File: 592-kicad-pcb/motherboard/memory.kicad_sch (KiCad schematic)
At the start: 11 parts, among them U11 SD Card Holder, U16 W25Q32JVZP

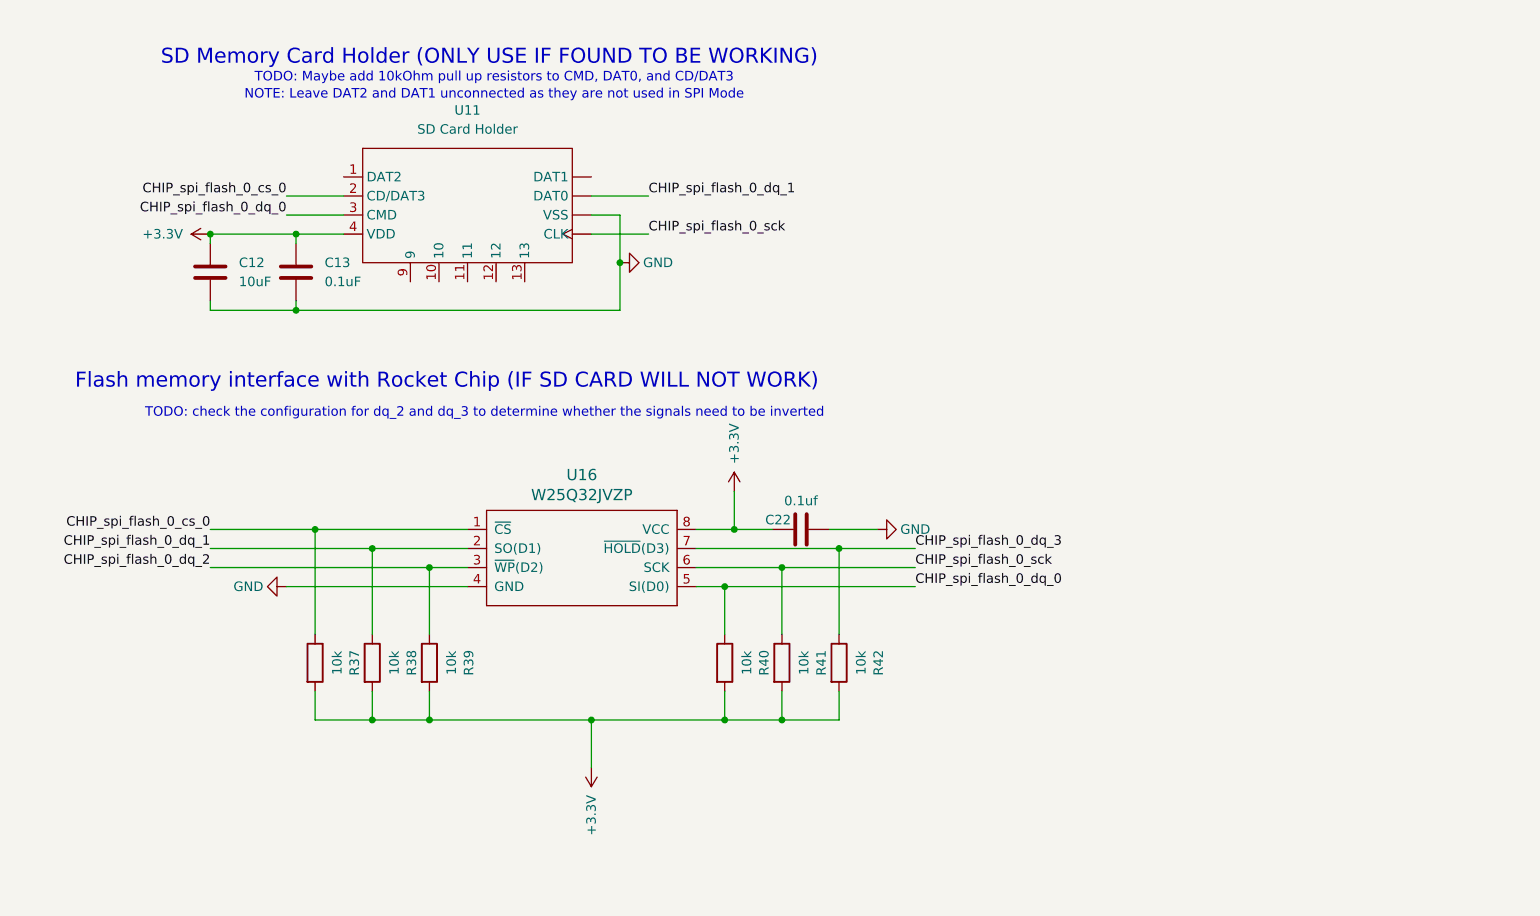
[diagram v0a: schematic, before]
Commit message: combine hierarchy of all sans power
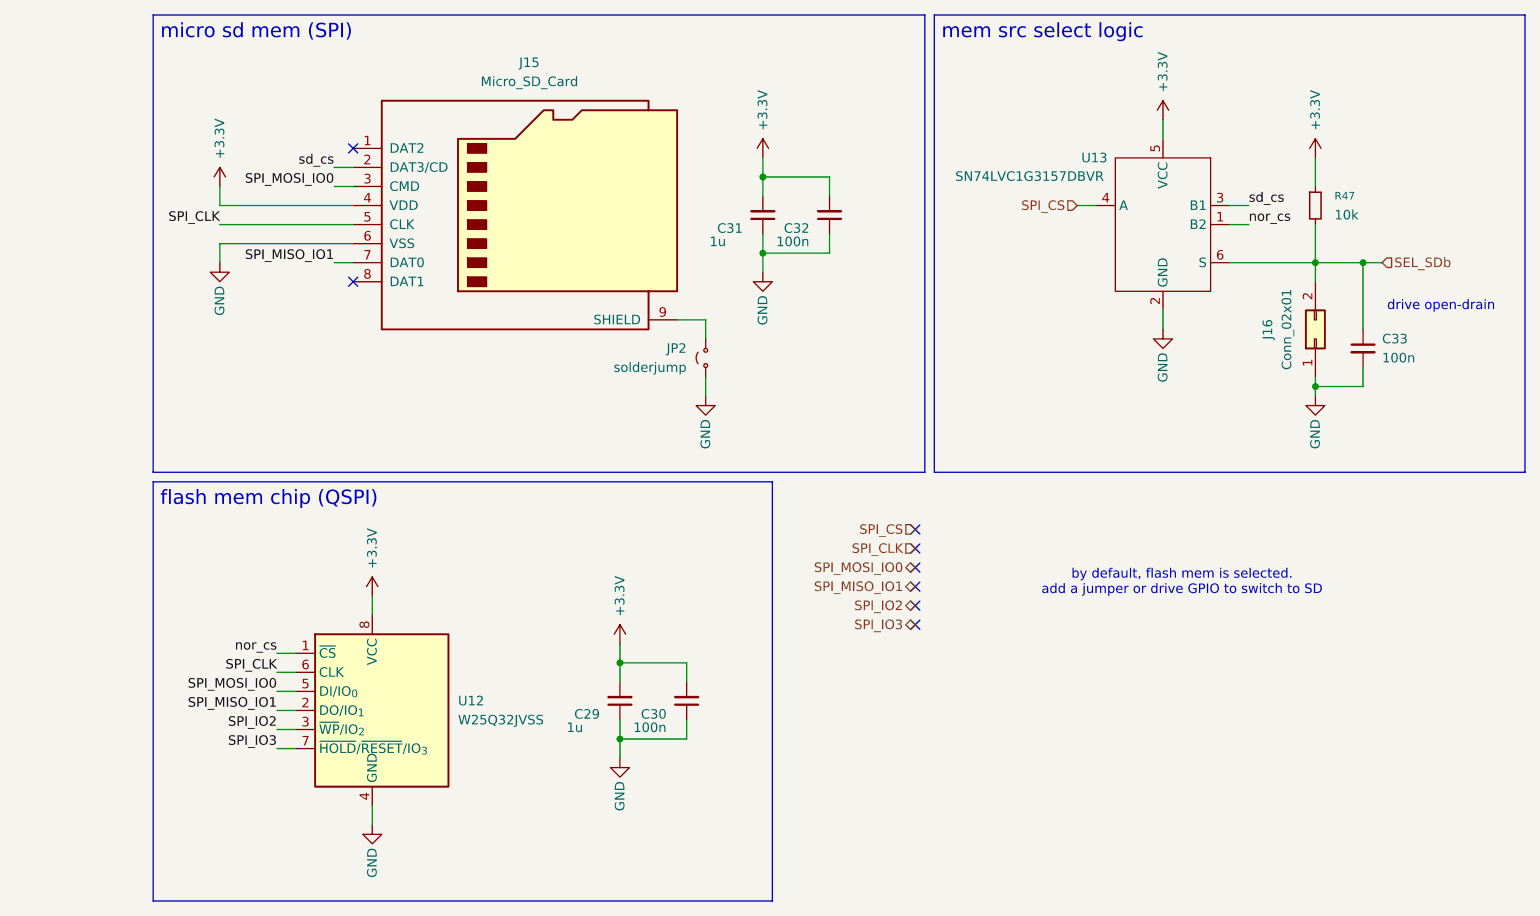
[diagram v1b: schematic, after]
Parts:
- removed C12: 10uF, symbol Device:C
- removed C13: 0.1uF, symbol Device:C
- removed C22: 0.1uf, Capacitor_SMD:C_0805_2012Metric, symbol Device:C
- removed R37, R38, R39, R40, R41, R42: 10k, Resistor_SMD:R_0805_2012Metric, symbol Device:R
- removed U11: SD Card Holder, symbol New_Library:sd_card_connector
- removed U16: W25Q32JVZP, strive_foot_prints:SOIC127P790X216-8N, symbol Caravel_board:W25Q32FVSS
- added C29, C31: 1u, symbol Device:C_Small
- added C30, C32, C33: 100n, symbol Device:C_Small
- added J15: Micro_SD_Card, symbol Connector:Micro_SD_Card
- added J16: Conn_02x01, symbol Connector_Generic:Conn_02x01
- added JP2: solderjump, symbol Jumper:Jumper_2_Small_Open
- added R47: 10k, symbol Device:R_Small
- added U12: W25Q32JVSS, Package_SO:SOIC-8_5.3x5.3mm_P1.27mm, symbol Memory_Flash:W25Q32JVSS
- added U13: SN74LVC1G3157DBVR, Package_TO_SOT_SMD:SOT-23-6, symbol 592-partslib:SN74LVC1G3157DBVR
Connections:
- net +3.3V: now also C29.2, C30.2, C31.2, C32.2, J15.4 (VDD), R47.1, U12.8 (VCC), U13.5 (VCC)
- net GND: now also C29.1, C30.1, C31.1, C32.1, C33.2, J15.6 (VSS), J16.1 (Pin_1), JP2.1 (A), U12.4 (GND), U13.2 (GND)
- new net: J15.9 (SHIELD), JP2.2 (B)
- new net SEL_SDb: C33.1, J16.2 (Pin_2), R47.2, U13.6 (S)
- new net SPI_CLK: J15.5 (CLK), U12.6 (CLK)
- new net SPI_CS: U13.4 (A)
- new net SPI_IO2: U12.3 (~{WP}/IO_{2})
- new net SPI_IO3: U12.7 (~{HOLD}/~{RESET}/IO_{3})
- new net SPI_MISO_IO1: J15.7 (DAT0), U12.2 (DO/IO_{1})
- new net SPI_MOSI_IO0: J15.3 (CMD), U12.5 (DI/IO_{0})
- new net nor_cs: U12.1 (~{CS}), U13.1 (B2)
- new net sd_cs: J15.2 (DAT3/CD), U13.3 (B1)
- no-connect marks 0 -> 8
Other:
- note added: "by default, flash mem is selected. add a jumper or drive GPIO to switch to SD"
- note added: "drive open-drain"
- note removed: "Flash memory interface with Rocket Chip (IF SD CARD WILL NOT WORK)"
- note removed: "NOTE: Leave DAT2 and DAT1 unconnected as they are not used in SPI Mode"
- note removed: "SD Memory Card Holder (ONLY USE IF FOUND TO BE WORKING)"
- note removed: "TODO: Maybe add 10kOhm pull up resistors to CMD, DAT0, and CD/DAT3"
- note removed: "TODO: check the configuration for dq_2 and dq_3 to determine whether the signals need to be inverted"

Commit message: partial update to use STM board, updated muxing of FTDI
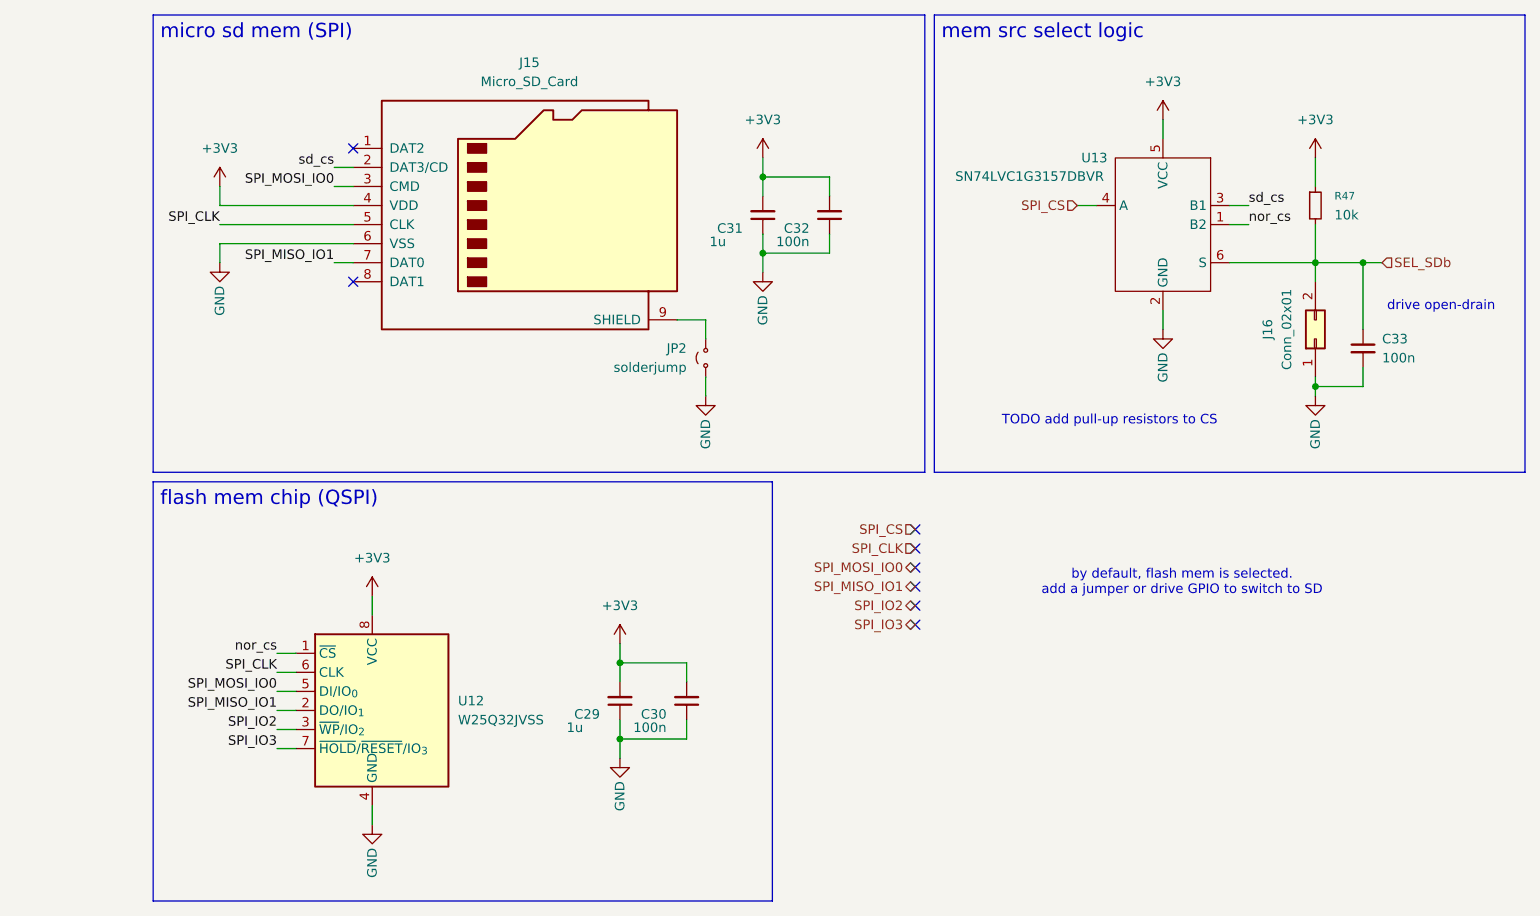
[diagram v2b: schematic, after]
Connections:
- net +3.3V renamed +3V3
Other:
- note added: "TODO add pull-up resistors to CS"

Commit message: update FTDI interfacing
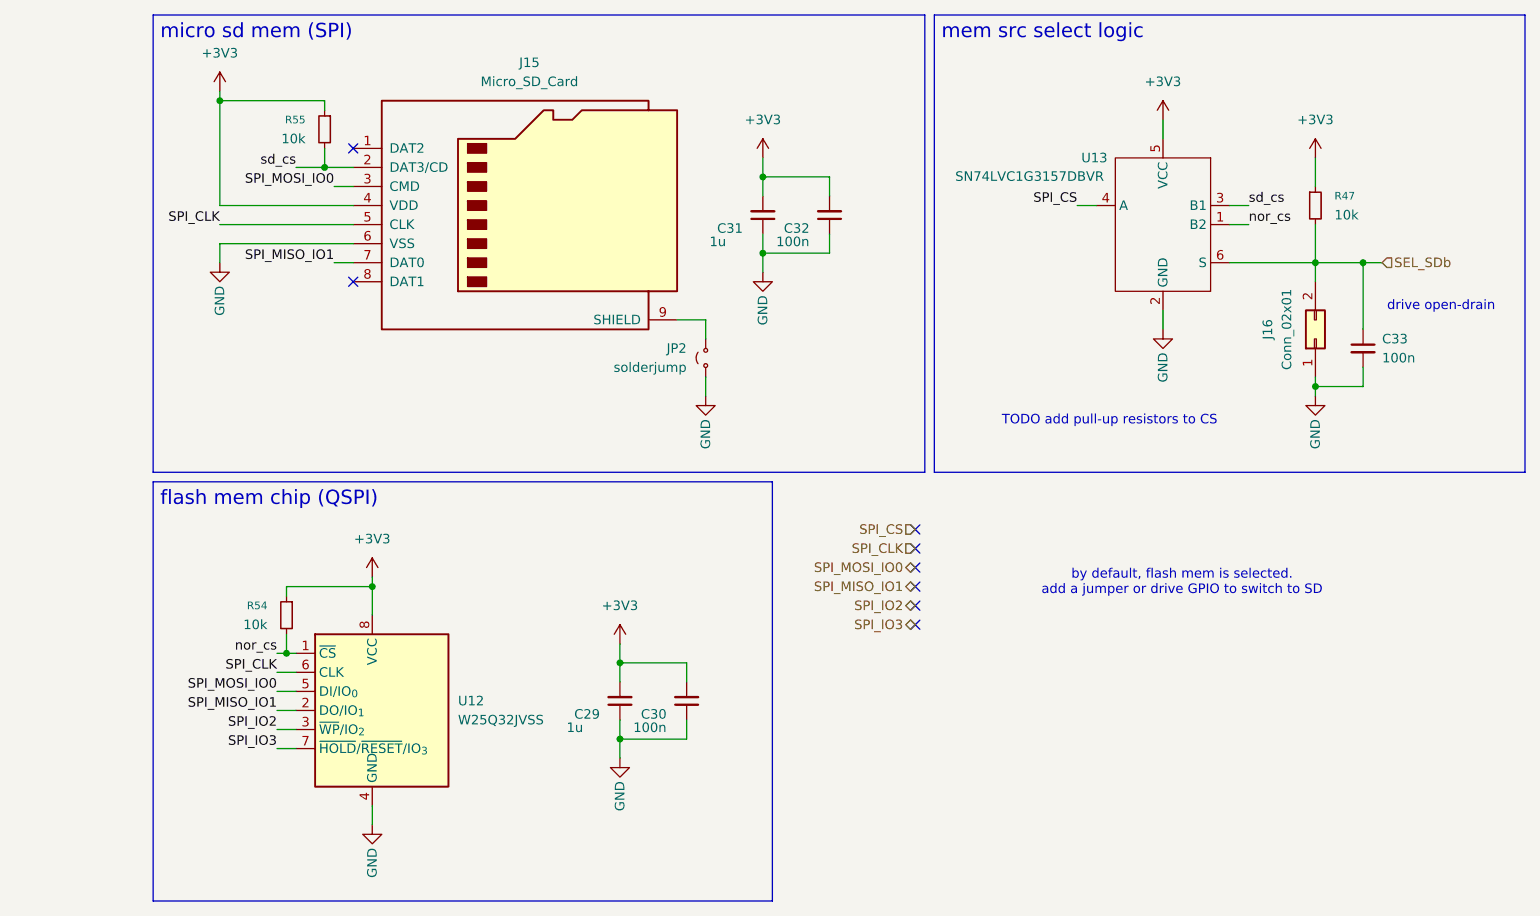
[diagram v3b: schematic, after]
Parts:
- added R54, R55: 10k, symbol Device:R_Small
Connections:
- net +3V3: now also R54.1, R55.1
- net nor_cs: now also R54.2
- net sd_cs: now also R55.2

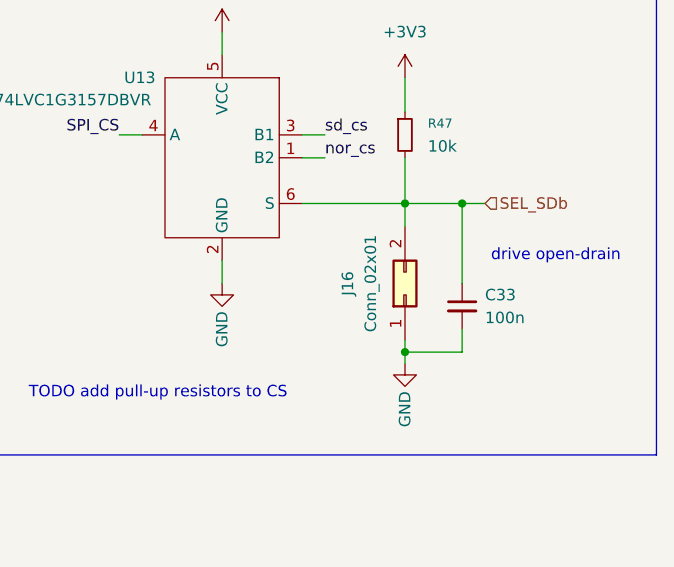
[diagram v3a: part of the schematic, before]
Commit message: add JLC part num for parts, footprints
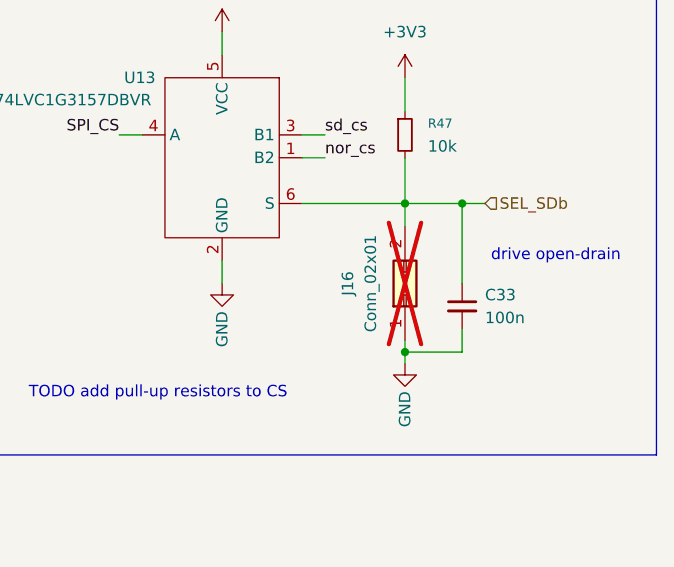
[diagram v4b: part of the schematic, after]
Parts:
- C29, C31: footprint (none) -> Capacitor_SMD:C_0603_1608Metric; LCSC (none) -> C15849
- C30, C32, C33: footprint (none) -> Capacitor_SMD:C_0402_1005Metric; LCSC (none) -> C1525
- J15: footprint (none) -> Connector_Card:microSD_HC_Hirose_DM3AT-SF-PEJM5; LCSC (none) -> C114218
- J16: footprint (none) -> Connector_PinHeader_1.27mm:PinHeader_1x02_P1.27mm_Vertical; now not fitted
- JP2: footprint (none) -> Jumper:SolderJumper-2_P1.3mm_Open_RoundedPad1.0x1.5mm
- R47, R54, R55: footprint (none) -> Resistor_SMD:R_0402_1005Metric; LCSC (none) -> C25744
- U12: LCSC (none) -> C82344
- U13: LCSC (none) -> C10426
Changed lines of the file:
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@@
 			)
 		)
-		(property "Footprint" ""
+		(property "Footprint" "Capacitor_SMD:C_0402_1005Metric"
 			(at 199.39 82.55 0)
 			(effects
@@
 			)
 		)
+		(property "LCSC" "C1525"
+			(at 199.39 82.55 0)
+			(effects
+				(font
+					(size 1.27 1.27)
+				)
+				(hide yes)
+			)
+		)
 		(pin "2"
 		)
@@
 			)
 		)
-		(property "Footprint" ""
+		(property "Footprint" "Capacitor_SMD:C_0603_1608Metric"
 			(at 119.38 64.77 0)
 			(effects
@@
 		)
 		(property "Description" "Unpolarized capacitor, small symbol"
+			(at 119.38 64.77 0)
+			(effects
+				(font
+					(size 1.27 1.27)
+				)
+				(hide yes)
+			)
+		)
+		(property "LCSC" "C15849"
 			(at 119.38 64.77 0)
 			(effects
@@
 			)
 		)
-		(property "Footprint" ""
+		(property "Footprint" "Resistor_SMD:R_0402_1005Metric"
 			(at 193.04 63.5 0)
 			(effects
@@
 			)
 		)
+		(property "LCSC" "C25744"
+			(at 193.04 63.5 0)
+			(effects
+				(font
+					(size 1.27 1.27)
+				)
+				(hide yes)
+			)
+		)
 		(pin "2"
 		)
@@
 			)
 		)
-		(property "Footprint" ""
+		(property "Footprint" "Capacitor_SMD:C_0603_1608Metric"
 			(at 100.33 129.54 0)
 			(effects
@@
 		)
 		(property "Description" "Unpolarized capacitor, small symbol"
+			(at 100.33 129.54 0)
+			(effects
+				(font
+					(size 1.27 1.27)
+				)
+				(hide yes)
+			)
+		)
+		(property "LCSC" "C15849"
 			(at 100.33 129.54 0)
 			(effects
@@
 			)
 		)
+		(property "LCSC" "C10426"
+			(at 172.72 66.04 0)
+			(effects
+				(font
+					(size 1.27 1.27)
+				)
+				(hide yes)
+			)
+		)
 		(pin "5"
 		)
@@
 			)
 		)
+		(property "LCSC" "C82344"
+			(at 67.31 130.81 0)
+			(effects
+				(font
+					(size 1.27 1.27)
+				)
+				(hide yes)
+			)
+		)
 		(pin "7"
 		)
@@
 			)
 		)
-		(property "Footprint" ""
+		(property "Footprint" "Connector_Card:microSD_HC_Hirose_DM3AT-SF-PEJM5"
 			(at 116.84 55.88 0)
 			(effects
@@
 			)
 		)
+		(property "LCSC" "C114218"
+			(at 87.63 63.5 0)
+			(effects
+				(font
+					(size 1.27 1.27)
+				)
+				(hide yes)
+			)
+		)
 		(pin "3"
 		)
@@
 			)
 		)
-		(property "Footprint" ""
+		(property "Footprint" "Jumper:SolderJumper-2_P1.3mm_Open_RoundedPad1.0x1.5mm"
 			(at 111.76 83.82 0)
 			(effects
@@
 		(in_bom yes)
 		(on_board yes)
-		(dnp no)
+		(dnp yes)
 		(fields_autoplaced yes)
 		(property "Reference" "J16"
@@
 			)
 		)
-		(property "Footprint" ""
+		(property "Footprint" "Connector_PinHeader_1.27mm:PinHeader_1x02_P1.27mm_Vertical"
 			(at 193.04 81.28 0)
 			(effects
@@
 			)
 		)
-		(property "Footprint" ""
+		(property "Footprint" "Capacitor_SMD:C_0402_1005Metric"
 			(at 109.22 129.54 0)
 			(effects
@@
 		)
 		(property "Description" "Unpolarized capacitor, small symbol"
+			(at 109.22 129.54 0)
+			(effects
+				(font
+					(size 1.27 1.27)
+				)
+				(hide yes)
+			)
+		)
+		(property "LCSC" "C1525"
 			(at 109.22 129.54 0)
 			(effects
@@
 			)
 		)
-		(property "Footprint" ""
+		(property "Footprint" "Resistor_SMD:R_0402_1005Metric"
 			(at 60.96 53.34 0)
 			(effects
@@
 			)
 		)
+		(property "LCSC" "C25744"
+			(at 60.96 53.34 0)
+			(effects
+				(font
+					(size 1.27 1.27)
+				)
+				(hide yes)
+			)
+		)
 		(pin "2"
 		)
@@
 			)
 		)
-		(property "Footprint" ""
+		(property "Footprint" "Capacitor_SMD:C_0402_1005Metric"
 			(at 128.27 64.77 0)
 			(effects
@@
 		)
 		(property "Description" "Unpolarized capacitor, small symbol"
+			(at 128.27 64.77 0)
+			(effects
+				(font
+					(size 1.27 1.27)
+				)
+				(hide yes)
+			)
+		)
+		(property "LCSC" "C1525"
 			(at 128.27 64.77 0)
 			(effects
@@
 			)
 		)
-		(property "Footprint" ""
+		(property "Footprint" "Resistor_SMD:R_0402_1005Metric"
 			(at 55.88 118.11 0)
 			(effects
@@
 			(at 55.88 118.11 0)
 			(effects
+				(font
+					(size 1.27 1.27)
+				)
+				(hide yes)
+			)
+		)
+		(property "LCSC" "C25744"
+			(at 55.88 118.11 0)
+			(effects
